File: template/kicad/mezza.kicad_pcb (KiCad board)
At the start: 2 copper layers, 85 x 54 mm, 6 parts, among them P1 CONN_02X20, P2 CONN_02X20

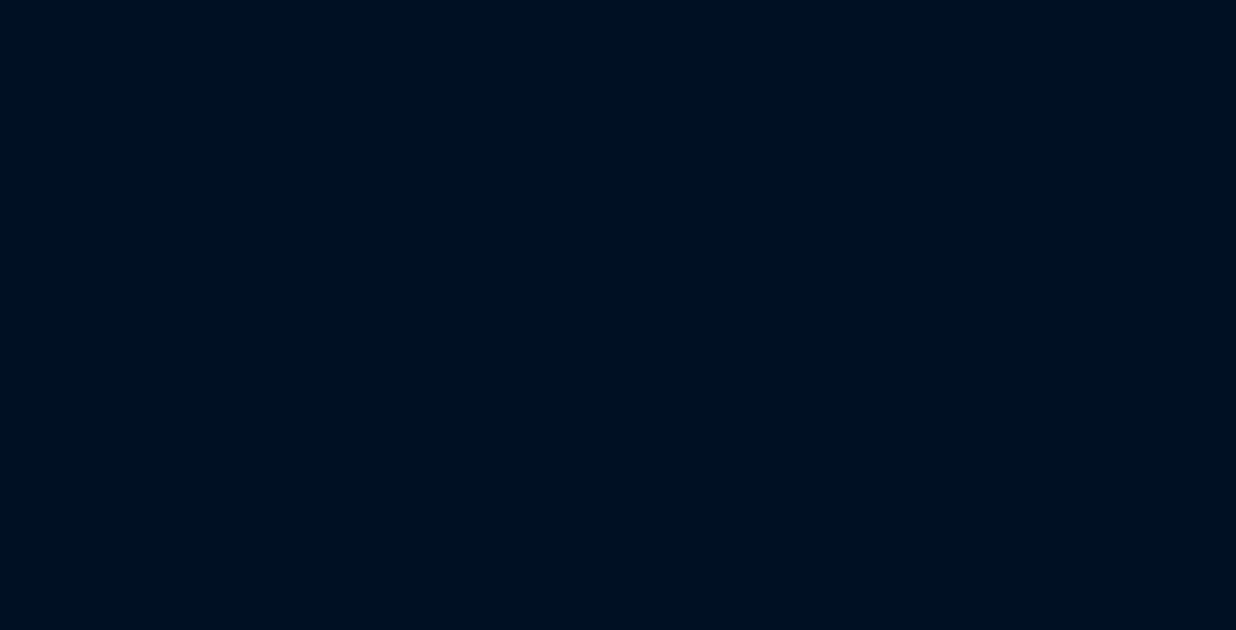
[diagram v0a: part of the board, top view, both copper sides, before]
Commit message: Add high speed connector to kicad template
Schematic connector added with net names.
3D model included for PCB footprint.

Signed-off-by: Michael Welling <mwelling@ieee.org>
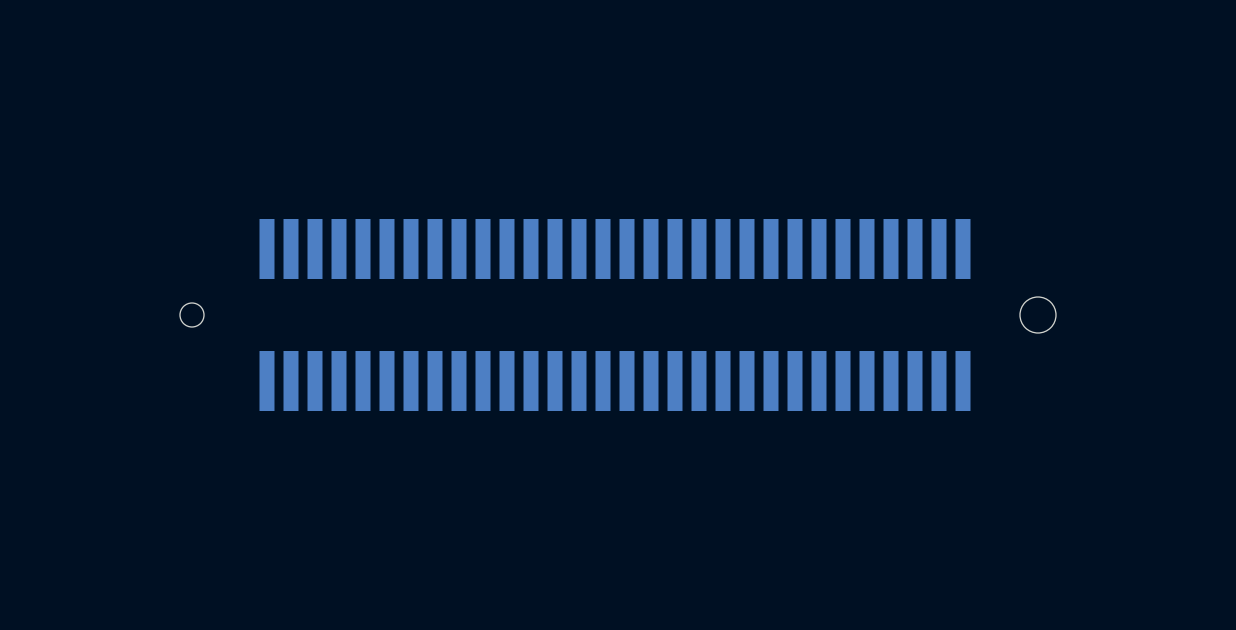
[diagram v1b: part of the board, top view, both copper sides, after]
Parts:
- added P3: CONN_02X30, 96boards:61083-063400LF, B.Cu at (132.8, 138.6)

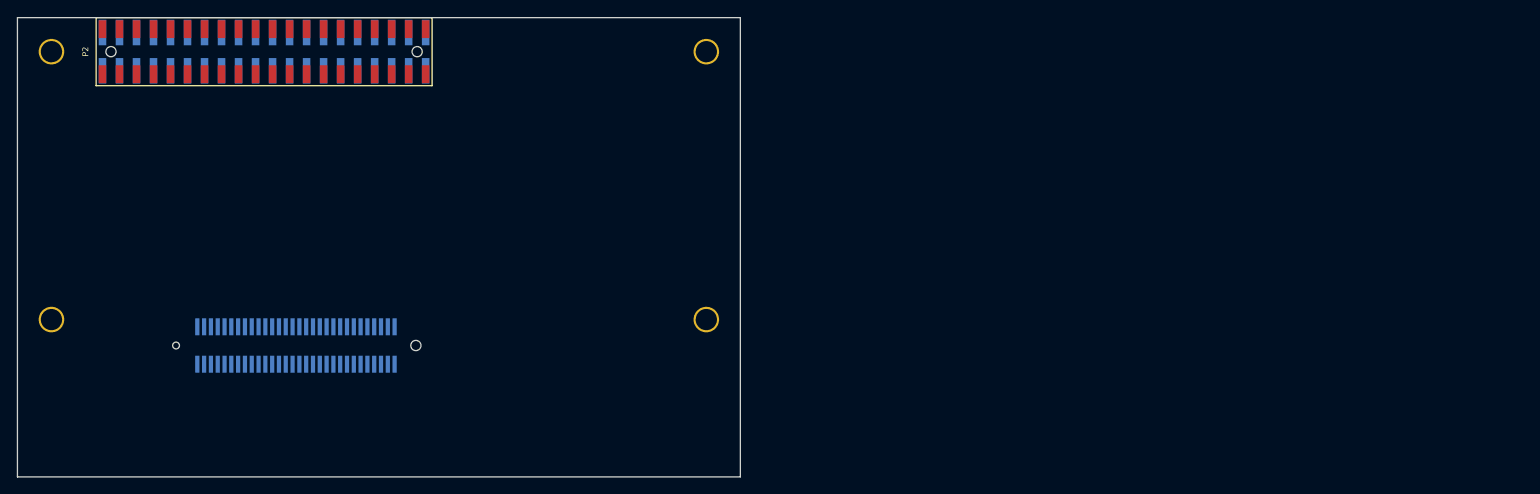
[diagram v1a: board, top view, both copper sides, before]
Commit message: KiCad template: Add footprints for CE form factors
Add footprints for each of the 96Boards CE form factors; standard,
extended-A and extended-B. The footprint contains the correct size and
position of the mounting holes, the position of each of the expansion
connectors, and the dimensions of the keepout areas. Adding one of these
footprints to a board design will make it much easier to make sure
everything is lined up correctly.

Also update the template PCB to use the standard size footprint instead
of discrete 1pin holes, and add a note about how to swap it for the
extended-A or -B footprint.

Signed-off-by: Grant Likely <grant.likely@secretlab.ca>
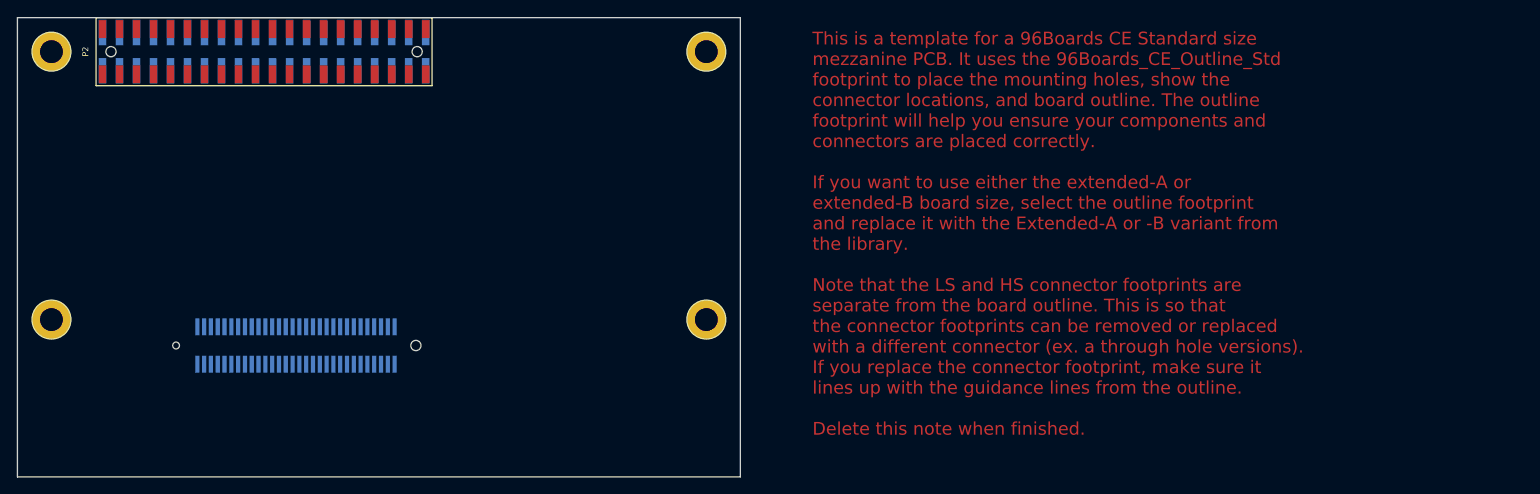
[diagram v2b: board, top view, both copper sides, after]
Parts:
- removed the REF** at (104.0, 135.5)
- removed the REF** at (181.0, 135.5)
- removed the REF** at (181.0, 104.0)
- removed the REF** at (104.0, 104.0)
- added REF**: 96Boards CE Outline Standard, 96boards:96Boards_CE_outline_std, F.Cu at (100.0, 154.0)
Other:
- board text added: "This is a template for a 96Boards CE Standard size mezzanine PCB. It uses the 96Boards_CE_Outline_Std footprint to place the mounting holes, show the connector locations, and board outline. The outline footprint will help you ensure your components and connectors are placed correctly. If you want to use either the extended-A or extended-B board size, select the outline footprint and replace it wi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"

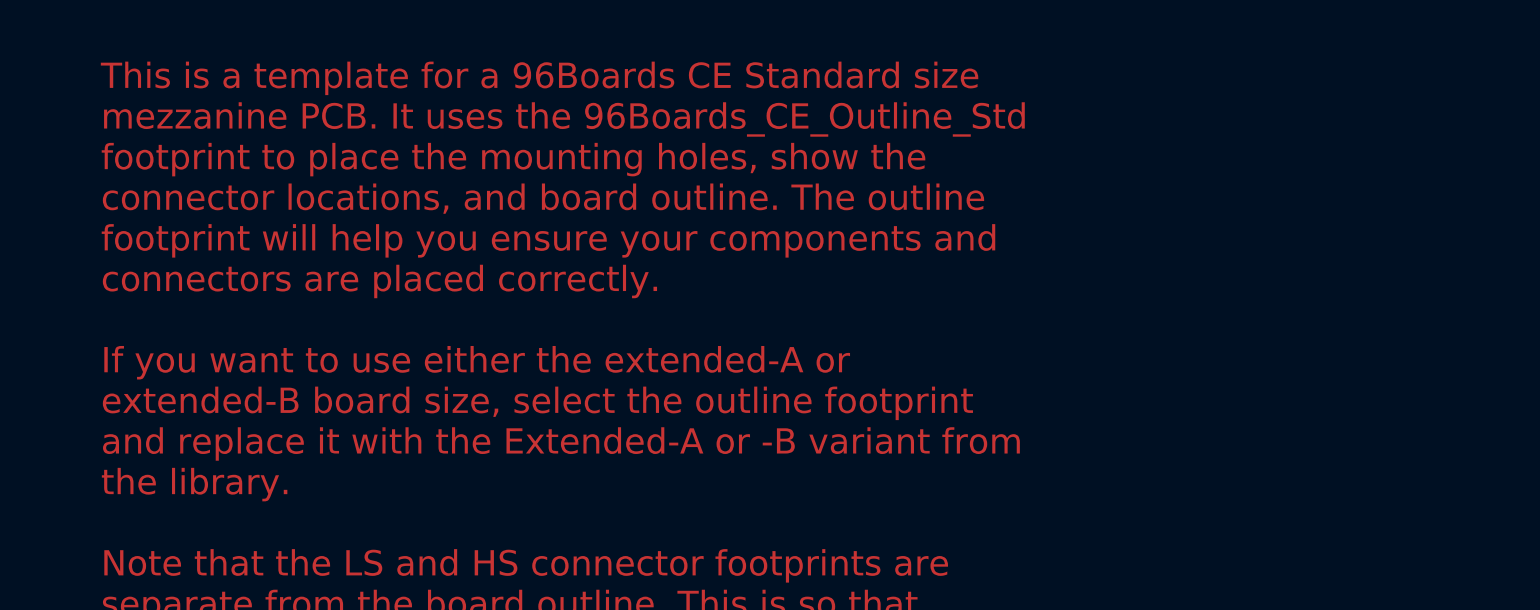
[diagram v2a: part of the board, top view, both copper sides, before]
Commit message: kicad: Merge extended A/B footprints into one
The extended A/B outlines are supposed to be the same size, but the
template showed extended A as being a smaller board. This happened due
to misreading the 96Boards CE spec. Fixed by deleting the Ext'd A template
and renaming the Ext'd B template to simply 96Boards_CE_outline_extd.
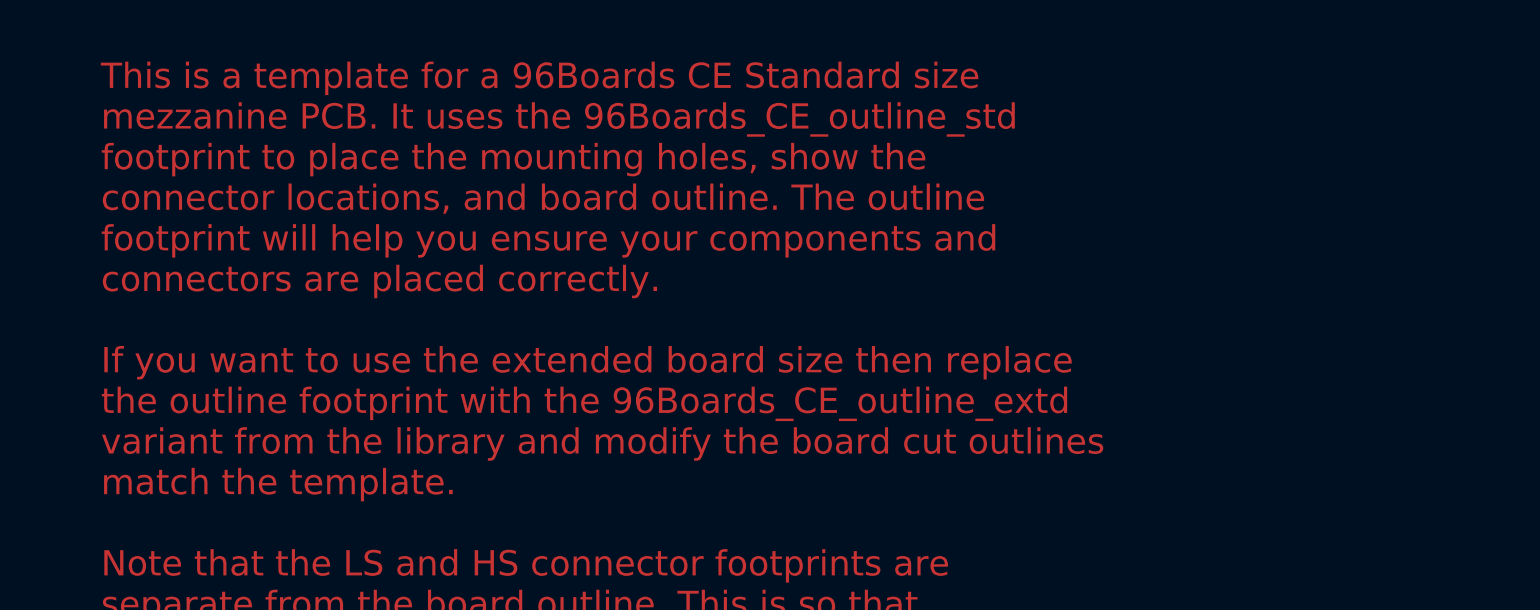
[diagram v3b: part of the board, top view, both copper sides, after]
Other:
- board text added: "This is a template for a 96Boards CE Standard size mezzanine PCB. It uses the 96Boards_CE_outline_std footprint to place the mounting holes, show the connector locations, and board outline. The outline footprint will help you ensure your components and connectors are placed correctly. If you want to use the extended board size then replace the outline footprint with the 96Boards_CE_outline_extd v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"
- board text removed: "This is a template for a 96Boards CE Standard size mezzanine PCB. It uses the 96Boards_CE_Outline_Std footprint to place the mounting holes, show the connector locations, and board outline. The outline footprint will help you ensure your components and connectors are placed correctly. If you want to use either the extended-A or extended-B board size, select the outline footprint and replace it wi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"
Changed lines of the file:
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@@
     (links 61)
     (no_connects 61)
-    (area 85.221429 87.3 185.252801 159.500001)
+    (area 85.221429 87.3 258.900572 159.500001)
     (thickness 1.6)
     (drawings 14)
@@
     )
   )
-  (gr_text "This is a template for a 96Boards CE Standard size\nmezzanine PCB. It uses the 96Boards_CE_Outline_Std\nfootprint to place the mounting holes, show the\nconnector locations, and board outline. The outline\nfootprint will help you ensure your components and\nconnectors are placed correctly.\n\nIf you want to use either the extended-A or\nextended-B board size, select the outline footprint\nand replace it with the Extended-A or -B variant from\nthe library.\n\nNote that the LS and HS connector footprints are\nseparate from the board outline. This is so that\nthe connector footprints can be removed or replaced\nwith a different connector (ex. a through hole versions).\nIf you replace the connector footprint, make sure it\nlines up with the guidance lines from the outline.\n\nDelete this note when finished." (at 193.472 125.4) (layer F.Cu)
+  (gr_text "This is a template for a 96Boards CE Standard size\nmezzanine PCB. It uses the 96Boards_CE_outline_std\nfootprint to place the mounting holes, show the\nconnector locations, and board outline. The outline\nfootprint will help you ensure your components and\nconnectors are placed correctly.\n\nIf you want to use the extended board size then replace\nthe outline footprint with the 96Boards_CE_outline_extd\nvariant from the library and modify the board cut outlines\nmatch the template.\n\nNote that the LS and HS connector footprints are\nseparate from the board outline. This is so that\nthe connector footprints can be removed or replaced\nwith a different connector (ex. a through hole versions).\nIf you replace the connector footprint, make sure it\nlines up with the guidance lines from the outline.\n\nDelete this note when finished." (at 193.472 125.4) (layer F.Cu)
     (effects (font (size 1.5 1.5) (thickness 0.3)) (justify left))
   )
